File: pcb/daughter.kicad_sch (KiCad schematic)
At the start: 0 parts

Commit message: moved stuff around
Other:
- sheet Module Bay 2 ports: added +3V3, GND; removed none
- sheet Module Bay 3 ports: added +3V3, GND; removed none

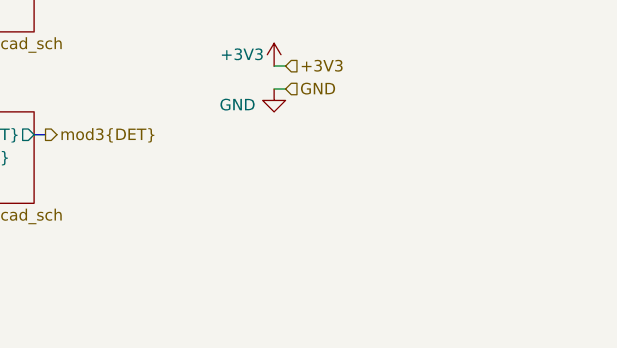
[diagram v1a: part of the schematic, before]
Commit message: finished daughter board, added stuff to main board
added esd and extra mounting hole to mainboard, finished daughter board
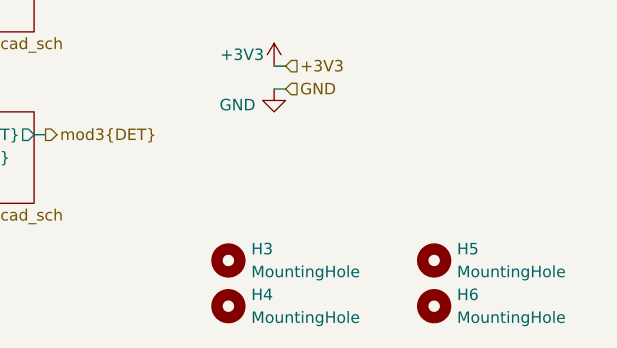
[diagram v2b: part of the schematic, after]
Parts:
- added H3, H4, H5, H6: MountingHole, MountingHole:MountingHole_2.2mm_M2, symbol Mechanical:MountingHole
